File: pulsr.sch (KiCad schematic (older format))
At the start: 8 parts, among them J1 JST_PH, J2 0.1\" header, Q1 FDN339AN

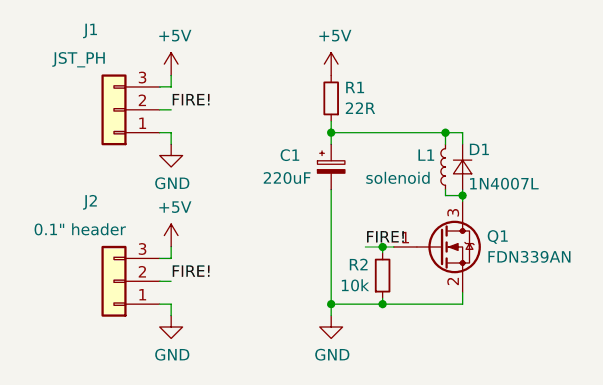
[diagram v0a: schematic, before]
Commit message: Modified design to fit 47mF super-cap
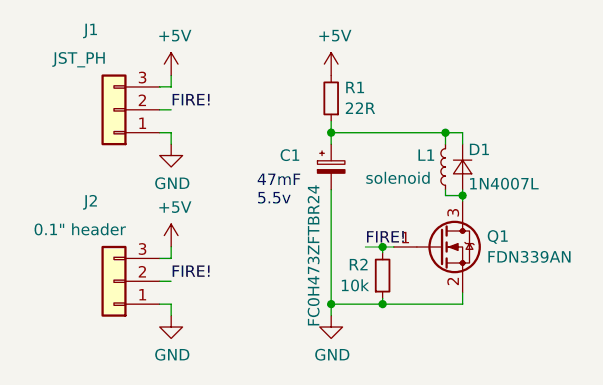
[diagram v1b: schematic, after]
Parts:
- C1: value 220uF -> FC0H473ZFTBR24; footprint Capacitor_SMD:CP_Elec_6.3x5.4 -> Capacitor_SMD:CP_Elec_10x10.5
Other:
- note added: "47mF\n5.5v"
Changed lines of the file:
@@
-EESchema Schematic File Version 5
+EESchema Schematic File Version 4
 LIBS:pulsr-cache
-EELAYER 30 0
+EELAYER 29 0
 EELAYER END
 $Descr A4 11693 8268
@@
 Comment3 ""
 Comment4 ""
-Comment5 ""
-Comment6 ""
-Comment7 ""
-Comment8 ""
-Comment9 ""
 $EndDescr
 $Comp
@@
 	-1   0    0    -1
 $EndComp
+Wire Wire Line
+	7325 2350 7325 2300
+Wire Wire Line
+	7325 2300 7400 2300
+Wire Wire Line
+	7400 2300 7400 2350
+Wire Wire Line
+	7400 2550 7400 2575
+Wire Wire Line
+	7400 2575 7325 2575
+Wire Wire Line
+	7325 2575 7325 2550
+$Comp
+L Device:Q_NMOS_GSD Q1
+U 1 1 5D7821F6
+P 7300 2800
+F 0 "Q1" H 7506 2846 50  0000 L CNN
+F 1 "FDN339AN" H 7506 2755 50  0000 L CNN
+F 2 "Package_TO_SOT_SMD:SOT-23_Handsoldering" H 7500 2900 50  0001 C CNN
+F 3 "~" H 7300 2800 50  0001 C CNN
+	1    7300 2800
+	1    0    0    -1
+$EndComp
+Wire Wire Line
+	7400 2600 7400 2575
+Connection ~ 7400 2575
+Connection ~ 7325 2300
+Wire Wire Line
+	7400 3050 7400 3000
+$Comp
+L Connector_Generic:Conn_01x03 J1
+U 1 1 5D79CF3B
+P 5875 2200
+F 0 "J1" H 5975 1850 50  0000 C CNN
+F 1 "JST_PH" H 6025 1975 50  0000 C CNN
+F 2 "Connector_JST:JST_PH_S3B-PH-K_1x03_P2.00mm_Horizontal" H 5875 2200 50  0001 C CNN
+F 3 "~" H 5875 2200 50  0001 C CNN
+	1    5875 2200
+	-1   0    0    1
+$EndComp
+Text Label 6975 2800 0    50   ~ 0
+FIRE!
+$Comp
+L Connector_Generic:Conn_01x03 J2
+U 1 1 5D7A4BD6
+P 5875 2950
+F 0 "J2" H 5975 2600 50  0000 C CNN
+F 1 "0.1\" header" H 6025 2725 50  0000 C CNN
+F 2 "Connector_PinHeader_2.54mm:PinHeader_1x03_P2.54mm_Vertical" H 5875 2950 50  0001 C CNN
+F 3 "~" H 5875 2950 50  0001 C CNN
+	1    5875 2950
+	-1   0    0    1
+$EndComp
+Wire Wire Line
+	7100 2800 7050 2800
+$Comp
+L power:+5V #PWR0103
+U 1 1 5D7AEA57
+P 6125 2050
+F 0 "#PWR0103" H 6125 1900 50  0001 C CNN
+F 1 "+5V" H 6140 2223 50  0000 C CNN
+F 2 "" H 6125 2050 50  0001 C CNN
+F 3 "" H 6125 2050 50  0001 C CNN
+	1    6125 2050
+	1    0    0    -1
+$EndComp
+$Comp
+L power:GND #PWR0104
+U 1 1 5D7AF3A8
+P 6125 2350
+F 0 "#PWR0104" H 6125 2100 50  0001 C CNN
+F 1 "GND" H 6130 2177 50  0000 C CNN
+F 2 "" H 6125 2350 50  0001 C CNN
+F 3 "" H 6125 2350 50  0001 C CNN
+	1    6125 2350
+	1    0    0    -1
+$EndComp
+Text Label 6125 2200 0    50   ~ 0
+FIRE!
+Wire Wire Line
+	6075 2200 6125 2200
+Wire Wire Line
+	6075 2300 6125 2300
+Wire Wire Line
+	6125 2300 6125 2350
+Wire Wire Line
+	6125 2050 6125 2100
+Wire Wire Line
+	6125 2100 6075 2100
+$Comp
+L power:+5V #PWR0105
+U 1 1 5D7B266C
+P 6125 2800
+F 0 "#PWR0105" H 6125 2650 50  0001 C CNN
+F 1 "+5V" H 6140 2973 50  0000 C CNN
+F 2 "" H 6125 2800 50  0001 C CNN
+F 3 "" H 6125 2800 50  0001 C CNN
+	1    6125 2800
+	1    0    0    -1
+$EndComp
+$Comp
+L power:GND #PWR0106
+U 1 1 5D7B2676
+P 6125 3100
+F 0 "#PWR0106" H 6125 2850 50  0001 C CNN
+F 1 "GND" H 6130 2927 50  0000 C CNN
+F 2 "" H 6125 3100 50  0001 C CNN
+F 3 "" H 6125 3100 50  0001 C CNN
+	1    6125 3100
+	1    0    0    -1
+$EndComp
+Text Label 6125 2950 0    50   ~ 0
+FIRE!
+Wire Wire Line
+	6075 2950 6125 2950
+Wire Wire Line
+	6075 3050 6125 3050
+Wire Wire Line
+	6125 3050 6125 3100
+Wire Wire Line
+	6125 2800 6125 2850
+Wire Wire Line
+	6125 2850 6075 2850
+$Comp
+L Device:R_Small R2
+U 1 1 5D89CC76
+P 7050 2925
+F 0 "R2" H 6991 2879 50  0000 R CNN
+F 1 "10k" H 6991 2970 50  0000 R CNN
+F 2 "Resistor_SMD:R_0603_1608Metric_Pad1.05x0.95mm_HandSolder" H 7050 2925 50  0001 C CNN
+F 3 "~" H 7050 2925 50  0001 C CNN
+	1    7050 2925
+	1    0    0    1
+$EndComp
+Wire Wire Line
+	7050 2825 7050 2800
+Connection ~ 7050 2800
+Wire Wire Line
+	7050 3025 7050 3050
+Connection ~ 7050 3050
+Wire Wire Line
+	7050 3050 7400 3050
+Wire Wire Line
+	6975 2800 7050 2800
+$Comp
+L power:GND #PWR0102
+U 1 1 5D7A03E8
+P 6825 3100
+F 0 "#PWR0102" H 6825 2850 50  0001 C CNN
+F 1 "GND" H 6830 2927 50  0000 C CNN
+F 2 "" H 6825 3100 50  0001 C CNN
+F 3 "" H 6825 3100 50  0001 C CNN
+	1    6825 3100
+	1    0    0    -1
+$EndComp
+$Comp
+L power:+5V #PWR0101
+U 1 1 5D79EB68
+P 6825 2050
+F 0 "#PWR0101" H 6825 1900 50  0001 C CNN
+F 1 "+5V" H 6840 2223 50  0000 C CNN
+F 2 "" H 6825 2050 50  0001 C CNN
+F 3 "" H 6825 2050 50  0001 C CNN
+	1    6825 2050
+	1    0    0    -1
+$EndComp
+$Comp
+L Device:CP_Small C1
+U 1 1 5D78C611
+P 6825 2450
+F 0 "C1" H 6600 2500 50  0000 L CNN
+F 1 "FC0H473ZFTBR24" V 6750 1750 50  0000 L CNN
+F 2 "Capacitor_SMD:CP_Elec_10x10.5" H 6825 2450 50  0001 C CNN
+F 3 "~" H 6825 2450 50  0001 C CNN
+	1    6825 2450
+	1    0    0    -1
+$EndComp
+$Comp
+L Device:R_Small R1
+U 1 1 5D78A0D3
+P 6825 2150
+F 0 "R1" H 6766 2104 50  0000 R CNN
+F 1 "22R" H 6766 2195 50  0000 R CNN
+F 2 "Resistor_SMD:R_1206_3216Metric_Pad1.42x1.75mm_HandSolder" H 6825 2150 50  0001 C CNN
+F 3 "~" H 6825 2150 50  0001 C CNN
+	1    6825 2150
+	-1   0    0    1
+$EndComp
+Wire Wire Line
+	6825 2550 6825 3050
+Wire Wire Line
+	6825 2250 6825 2300
+Wire Wire Line
+	6825 3050 7050 3050
+Connection ~ 6825 3050
+Wire Wire Line
+	6825 3050 6825 3100
+Wire Wire Line
+	6825 2300 7325 2300
+Connection ~ 6825 2300
+Wire Wire Line
+	6825 2300 6825 2350
+Text Notes 6500 2625 0    50   ~ 0
+47mF\n5.5v
 $Comp
 L Device:D_Small D1
@@
 	0    -1   1    0
 $EndComp
-Wire Wire Line
-	7325 2350 7325 2300
-Wire Wire Line
-	7325 2300 7400 2300
-Wire Wire Line
-	7400 2300 7400 2350
-Wire Wire Line
-	7400 2550 7400 2575
-Wire Wire Line
-	7400 2575 7325 2575
-Wire Wire Line
-	7325 2575 7325 2550
-$Comp
-L Device:Q_NMOS_GSD Q1
-U 1 1 5D7821F6
-P 7300 2800
-F 0 "Q1" H 7506 2846 50  0000 L CNN
-F 1 "FDN339AN" H 7506 2755 50  0000 L CNN
-F 2 "Package_TO_SOT_SMD:SOT-23_Handsoldering" H 7500 2900 50  0001 C CNN
-F 3 "~" H 7300 2800 50  0001 C CNN
-	1    7300 2800
-	1    0    0    -1
-$EndComp
-Wire Wire Line
-	7400 2600 7400 2575
-Connection ~ 7400 2575
-Connection ~ 7325 2300
-Wire Wire Line
-	7400 3050 7400 3000
-$Comp
-L Connector_Generic:Conn_01x03 J1
-U 1 1 5D79CF3B
-P 5875 2200
-F 0 "J1" H 5975 1850 50  0000 C CNN
-F 1 "JST_PH" H 6025 1975 50  0000 C CNN
-F 2 "Connector_JST:JST_PH_S3B-PH-K_1x03_P2.00mm_Horizontal" H 5875 2200 50  0001 C CNN
-F 3 "~" H 5875 2200 50  0001 C CNN
-	1    5875 2200
-	-1   0    0    1
-$EndComp
-Text Label 6975 2800 0    50   ~ 0
-FIRE!
-$Comp
-L Connector_Generic:Conn_01x03 J2
-U 1 1 5D7A4BD6
-P 5875 2950
-F 0 "J2" H 5975 2600 50  0000 C CNN
-F 1 "0.1\" header" H 6025 2725 50  0000 C CNN
-F 2 "Connector_PinHeader_2.54mm:PinHeader_1x03_P2.54mm_Vertical" H 5875 2950 50  0001 C CNN
-F 3 "~" H 5875 2950 50  0001 C CNN
-	1    5875 2950
-	-1   0    0    1
-$EndComp
-Wire Wire Line
-	7100 2800 7050 2800
-$Comp
-L power:+5V #PWR0103
-U 1 1 5D7AEA57
-P 6125 2050
-F 0 "#PWR0103" H 6125 1900 50  0001 C CNN
-F 1 "+5V" H 6140 2223 50  0000 C CNN
-F 2 "" H 6125 2050 50  0001 C CNN
-F 3 "" H 6125 2050 50  0001 C CNN
-	1    6125 2050
-	1    0    0    -1
-$EndComp
-$Comp
-L power:GND #PWR0104
-U 1 1 5D7AF3A8
-P 6125 2350
-F 0 "#PWR0104" H 6125 2100 50  0001 C CNN
-F 1 "GND" H 6130 2177 50  0000 C CNN
-F 2 "" H 6125 2350 50  0001 C CNN
-F 3 "" H 6125 2350 50  0001 C CNN
-	1    6125 2350
-	1    0    0    -1
-$EndComp
-Text Label 6125 2200 0    50   ~ 0
-FIRE!
-Wire Wire Line
-	6075 2200 6125 2200
-Wire Wire Line
-	6075 2300 6125 2300
-Wire Wire Line
-	6125 2300 6125 2350
-Wire Wire Line
-	6125 2050 6125 2100
-Wire Wire Line
-	6125 2100 6075 2100
-$Comp
-L power:+5V #PWR0105
-U 1 1 5D7B266C
-P 6125 2800
-F 0 "#PWR0105" H 6125 2650 50  0001 C CNN
-F 1 "+5V" H 6140 2973 50  0000 C CNN
-F 2 "" H 6125 2800 50  0001 C CNN
-F 3 "" H 6125 2800 50  0001 C CNN
-	1    6125 2800
-	1    0    0    -1
-$EndComp
-$Comp
-L power:GND #PWR0106
-U 1 1 5D7B2676
-P 6125 3100
-F 0 "#PWR0106" H 6125 2850 50  0001 C CNN
-F 1 "GND" H 6130 2927 50  0000 C CNN
-F 2 "" H 6125 3100 50  0001 C CNN
-F 3 "" H 6125 3100 50  0001 C CNN
-	1    6125 3100
-	1    0    0    -1
-$EndComp
-Text Label 6125 2950 0    50   ~ 0
-FIRE!
-Wire Wire Line
-	6075 2950 6125 2950
-Wire Wire Line
-	6075 3050 6125 3050
-Wire Wire Line
-	6125 3050 6125 3100
-Wire Wire Line
-	6125 2800 6125 2850
-Wire Wire Line
-	6125 2850 6075 2850
-$Comp
-L Device:R_Small R2
-U 1 1 5D89CC76
-P 7050 2925
-F 0 "R2" H 6991 2879 50  0000 R CNN
-F 1 "10k" H 6991 2970 50  0000 R CNN
-F 2 "Resistor_SMD:R_0603_1608Metric_Pad1.05x0.95mm_HandSolder" H 7050 2925 50  0001 C CNN
-F 3 "~" H 7050 2925 50  0001 C CNN
-	1    7050 2925
-	1    0    0    1
-$EndComp
-Wire Wire Line
-	7050 2825 7050 2800
-Connection ~ 7050 2800
-Wire Wire Line
-	7050 3025 7050 3050
-Connection ~ 7050 3050
-Wire Wire Line
-	7050 3050 7400 3050
-Wire Wire Line
-	6975 2800 7050 2800
-$Comp
-L power:GND #PWR0102
-U 1 1 5D7A03E8
-P 6825 3100
-F 0 "#PWR0102" H 6825 2850 50  0001 C CNN
-F 1 "GND" H 6830 2927 50  0000 C CNN
-F 2 "" H 6825 3100 50  0001 C CNN
-F 3 "" H 6825 3100 50  0001 C CNN
-	1    6825 3100
-	1    0    0    -1
-$EndComp
-$Comp
-L power:+5V #PWR0101
-U 1 1 5D79EB68
-P 6825 2050
-F 0 "#PWR0101" H 6825 1900 50  0001 C CNN
-F 1 "+5V" H 6840 2223 50  0000 C CNN
-F 2 "" H 6825 2050 50  0001 C CNN
-F 3 "" H 6825 2050 50  0001 C CNN
-	1    6825 2050
-	1    0    0    -1
-$EndComp
-$Comp
-L Device:CP_Small C1
-U 1 1 5D78C611
-P 6825 2450
-F 0 "C1" H 6600 2500 50  0000 L CNN
-F 1 "220uF" H 6525 2400 50  0000 L CNN
-F 2 "Capacitor_SMD:CP_Elec_6.3x5.4" H 6825 2450 50  0001 C CNN
-F 3 "~" H 6825 2450 50  0001 C CNN
-	1    6825 2450
-	1    0    0    -1
-$EndComp
-$Comp
-L Device:R_Small R1
-U 1 1 5D78A0D3
-P 6825 2150
-F 0 "R1" H 6766 2104 50  0000 R CNN
-F 1 "22R" H 6766 2195 50  0000 R CNN
-F 2 "Resistor_SMD:R_1206_3216Metric_Pad1.42x1.75mm_HandSolder" H 6825 2150 50  0001 C CNN
-F 3 "~" H 6825 2150 50  0001 C CNN
-	1    6825 2150
-	-1   0    0    1
-$EndComp
-Wire Wire Line
-	6825 2550 6825 3050
-Wire Wire Line
-	6825 2250 6825 2300
-Wire Wire Line
-	6825 3050 7050 3050
-Connection ~ 6825 3050
-Wire Wire Line
-	6825 3050 6825 3100
-Wire Wire Line
-	6825 2300 7325 2300
-Connection ~ 6825 2300
-Wire Wire Line
-	6825 2300 6825 2350
 $EndSCHEMATC
